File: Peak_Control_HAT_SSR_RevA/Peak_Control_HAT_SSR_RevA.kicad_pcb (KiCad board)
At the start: 4 copper layers, 115 x 70 mm, 19 parts, among them J1 Raspberry Pi 40-pin stacking 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, J11 I2C: 3V3 / GND / SDA / SCL, J2 24V IN: +24V / 0V, J3 PROJECTOR: SW+24V / 0V, J4 VIEWER: SW+24V / 0V, J5 AUX1: SW+24V / 0V, J6 AUX2: SW+24V / 0V, U1 G3VM-61GR2, U2 G3VM-61GR2, U3 G3VM-61GR2, U4 G3VM-61GR2

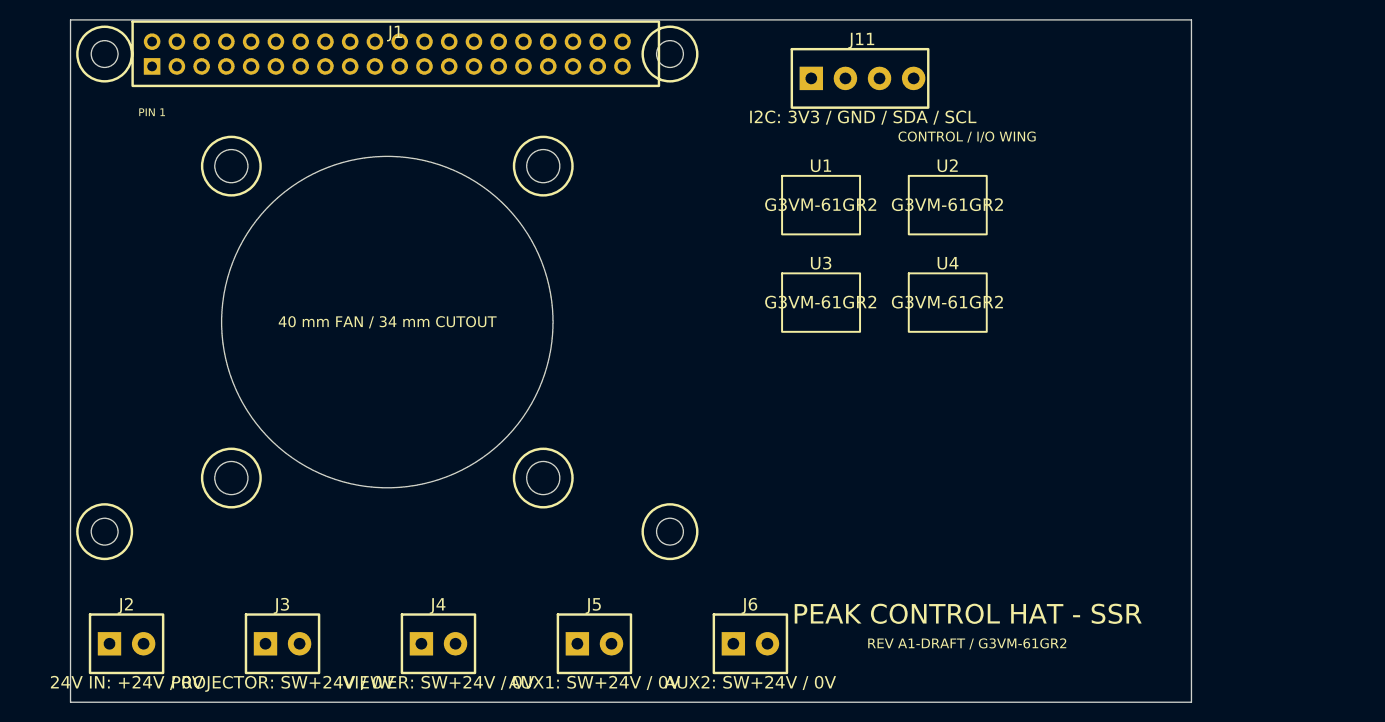
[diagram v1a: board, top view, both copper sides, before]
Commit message: Finalized Rev A component placement before routing
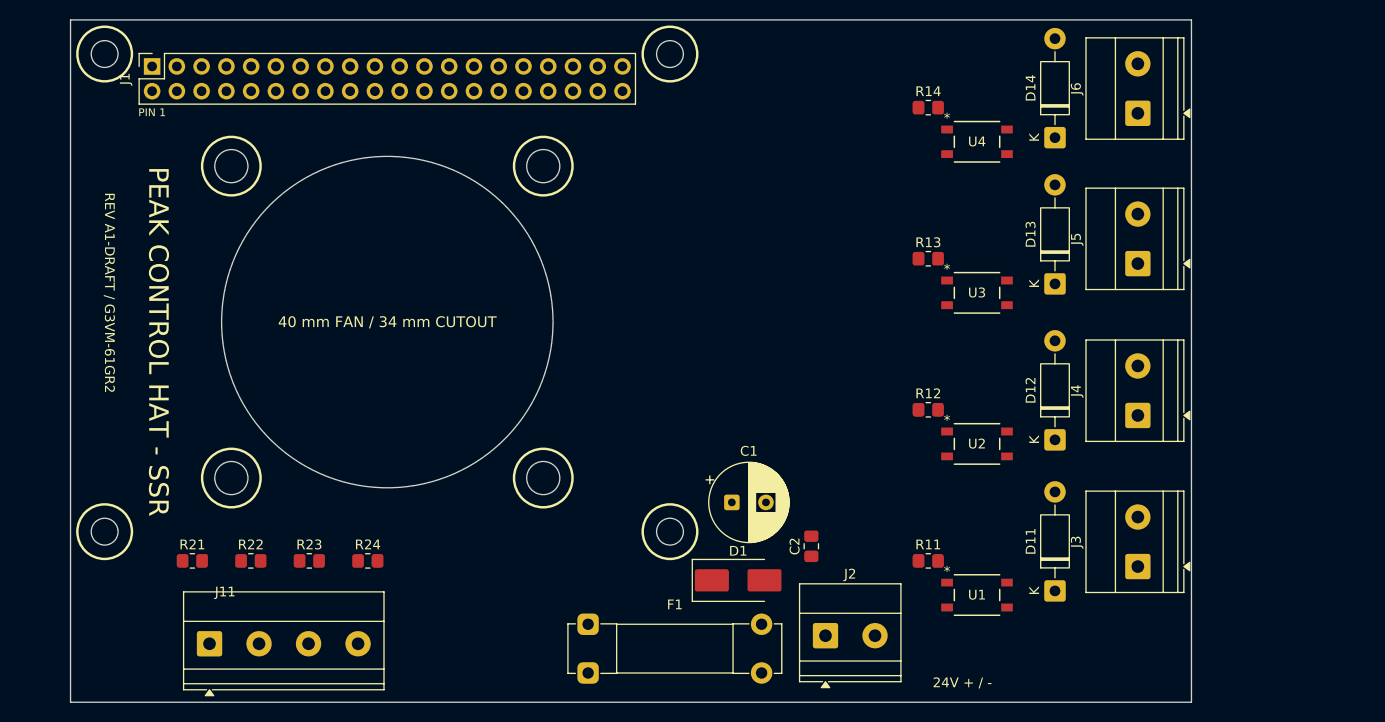
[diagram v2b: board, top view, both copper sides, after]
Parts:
- added C1: 47uF/50V, Capacitor_THT:CP_Radial_D8.0mm_P3.50mm, F.Cu at (67.8, 49.5)
- added C2: 1uF/50V, Capacitor_SMD:C_0805_2012Metric_Pad1.18x1.45mm_HandSolder, F.Cu at (76.0, 54.0)
- added D1: SMBJ33A, Diode_SMD:D_SMB_Handsoldering, F.Cu at (68.5, 57.5)
- added D11: 1N4007, Diode_THT:D_DO-41_SOD81_P10.16mm_Horizontal, F.Cu at (101.0, 58.6)
- added D12: 1N4007, Diode_THT:D_DO-41_SOD81_P10.16mm_Horizontal, F.Cu at (101.0, 43.1)
- added D13: 1N4007, Diode_THT:D_DO-41_SOD81_P10.16mm_Horizontal, F.Cu at (101.0, 27.1)
- added D14: 1N4007, Diode_THT:D_DO-41_SOD81_P10.16mm_Horizontal, F.Cu at (101.0, 12.1)
- added F1: 3A, Fuse:Fuseholder_Clip-5x20mm_Bel_FC-203-22_Lateral_P17.80x5.00mm_D1.17mm_Horizontal, F.Cu at (53.1, 62.0)
- added R11: 390R, Resistor_SMD:R_0805_2012Metric_Pad1.20x1.40mm_HandSolder, F.Cu at (88.0, 55.5)
- added R12: 390R, Resistor_SMD:R_0805_2012Metric_Pad1.20x1.40mm_HandSolder, F.Cu at (88.0, 40.0)
- added R13: 390R, Resistor_SMD:R_0805_2012Metric_Pad1.20x1.40mm_HandSolder, F.Cu at (88.0, 24.5)
- added R14: 390R, Resistor_SMD:R_0805_2012Metric_Pad1.20x1.40mm_HandSolder, F.Cu at (88.0, 9.00)
- added R21: DNP 4.7k SDA PU, Resistor_SMD:R_0805_2012Metric_Pad1.20x1.40mm_HandSolder, F.Cu at (12.5, 55.5)
- added R22: DNP 4.7k SCL PU, Resistor_SMD:R_0805_2012Metric_Pad1.20x1.40mm_HandSolder, F.Cu at (18.5, 55.5)
- added R23: 0R/optional 33-100R SDA, Resistor_SMD:R_0805_2012Metric_Pad1.20x1.40mm_HandSolder, F.Cu at (24.5, 55.5)
- added R24: 0R/optional 33-100R SCL, Resistor_SMD:R_0805_2012Metric_Pad1.20x1.40mm_HandSolder, F.Cu at (30.5, 55.5)
- J1: value Raspberry Pi 40-pin stacking header -> Raspberry Pi 40-Pin GPIO Header; footprint Peak:Raspberry_Pi_2x20_Header -> Connector_PinSocket_2.54mm:PinSocket_2x20_P2.54mm_Vertical
- J11: value I2C: 3V3 / GND / SDA / SCL -> I2C_EXPANSION; footprint Peak:Pluggable_Terminal_4P_3.5mm -> TerminalBlock_Phoenix:TerminalBlock_Phoenix_MKDS-1,5-4-5.08_1x04_P5.08mm_Horizontal
- J2: value 24V IN: +24V / 0V -> 24V_IN; footprint Peak:Pluggable_Terminal_2P_3.5mm -> TerminalBlock_Phoenix:TerminalBlock_Phoenix_MKDS-1,5-2-5.08_1x02_P5.08mm_Horizontal
- J3: value PROJECTOR: SW+24V / 0V -> PROJECTOR_SW24V_GND; footprint Peak:Pluggable_Terminal_2P_3.5mm -> TerminalBlock_Phoenix:TerminalBlock_Phoenix_MKDS-1,5-2-5.08_1x02_P5.08mm_Horizontal
- J4: value VIEWER: SW+24V / 0V -> VIEWER_SW24V_GND; footprint Peak:Pluggable_Terminal_2P_3.5mm -> TerminalBlock_Phoenix:TerminalBlock_Phoenix_MKDS-1,5-2-5.08_1x02_P5.08mm_Horizontal
- J5: value AUX1: SW+24V / 0V -> AUX1_SW24V_GND; footprint Peak:Pluggable_Terminal_2P_3.5mm -> TerminalBlock_Phoenix:TerminalBlock_Phoenix_MKDS-1,5-2-5.08_1x02_P5.08mm_Horizontal
- J6: value AUX2: SW+24V / 0V -> AUX2_SW24V_GND; footprint Peak:Pluggable_Terminal_2P_3.5mm -> TerminalBlock_Phoenix:TerminalBlock_Phoenix_MKDS-1,5-2-5.08_1x02_P5.08mm_Horizontal
- U1, U2, U3, U4: footprint Peak:G3VM-61GR2_PLACEHOLDER -> Omron:G-SOP4_OMR
- moved J3 89.8 mm to (109.5, 56.1), turned to 90 degrees
- moved J11 84.7 mm to (14.3, 64.0)
- moved J4 77.1 mm to (109.5, 40.6), turned to 90 degrees
- moved J2 73.5 mm to (77.5, 63.2)
- moved J5 69.5 mm to (109.5, 25.0), turned to 90 degrees
- moved J6 68.4 mm to (109.5, 9.58), turned to 90 degrees
- moved U1 40.8 mm to (89.9, 57.7)
- moved U2 23.2 mm to (89.9, 42.2)
- moved U4 17.8 mm to (89.9, 11.2)
- moved U3 13.1 mm to (89.9, 26.7)
- turned J1 to 90 degrees
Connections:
- J1 pad 1: (no net) -> /+3V3_PI
- J1 pad 10: (no net) -> unconnected-(J1-Pin_10-Pad10)
- J1 pad 11: (no net) -> unconnected-(J1-Pin_11-Pad11)
- J1 pad 12: (no net) -> unconnected-(J1-Pin_12-Pad12)
- J1 pad 13: (no net) -> unconnected-(J1-Pin_13-Pad13)
- J1 pad 14: (no net) -> /PI_GND
- J1 pad 15: (no net) -> /GPIO22_OUT3
- J1 pad 16: (no net) -> /GPIO23_OUT4
- J1 pad 17: (no net) -> unconnected-(J1-Pin_17-Pad17)
- J1 pad 18: (no net) -> unconnected-(J1-Pin_18-Pad18)
- J1 pad 19: (no net) -> unconnected-(J1-Pin_19-Pad19)
- J1 pad 2: (no net) -> unconnected-(J1-Pin_2-Pad2)
- J1 pad 20: (no net) -> /PI_GND
- J1 pad 21: (no net) -> unconnected-(J1-Pin_21-Pad21)
- J1 pad 22: (no net) -> unconnected-(J1-Pin_22-Pad22)
- J1 pad 23: (no net) -> unconnected-(J1-Pin_23-Pad23)
- J1 pad 24: (no net) -> unconnected-(J1-Pin_24-Pad24)
- J1 pad 25: (no net) -> /PI_GND
- J1 pad 26: (no net) -> unconnected-(J1-Pin_26-Pad26)
- J1 pad 27: (no net) -> unconnected-(J1-Pin_27-Pad27)
- J1 pad 28: (no net) -> unconnected-(J1-Pin_28-Pad28)
- J1 pad 29: (no net) -> unconnected-(J1-Pin_29-Pad29)
- J1 pad 3: (no net) -> /I2C_SDA_GPIO2
- J1 pad 30: (no net) -> /PI_GND
- J1 pad 31: (no net) -> unconnected-(J1-Pin_31-Pad31)
- J1 pad 32: (no net) -> unconnected-(J1-Pin_32-Pad32)
- J1 pad 33: (no net) -> unconnected-(J1-Pin_33-Pad33)
- J1 pad 34: (no net) -> /PI_GND
- J1 pad 35: (no net) -> /GPIO19_OUT2
- J1 pad 36: (no net) -> /GPIO16_OUT1
- J1 pad 37: (no net) -> unconnected-(J1-Pin_37-Pad37)
- J1 pad 38: (no net) -> unconnected-(J1-Pin_38-Pad38)
- J1 pad 39: (no net) -> /PI_GND
- J1 pad 4: (no net) -> unconnected-(J1-Pin_4-Pad4)
- J1 pad 40: (no net) -> unconnected-(J1-Pin_40-Pad40)
- J1 pad 5: (no net) -> /I2C_SCL_GPIO3
- J1 pad 6: (no net) -> /PI_GND
- J1 pad 7: (no net) -> unconnected-(J1-Pin_7-Pad7)
- J1 pad 8: (no net) -> unconnected-(J1-Pin_8-Pad8)
- J1 pad 9: (no net) -> /PI_GND
- J11 pad 1: (no net) -> /+3V3_PI
- J11 pad 2: (no net) -> /PI_GND
- J11 pad 3: (no net) -> /I2C_SDA_EXT
- J11 pad 4: (no net) -> /I2C_SCL_EXT
- J2 pad 1: (no net) -> Net-(J2-Pin_1)
- J2 pad 2: (no net) -> /FIELD_GND
- J3 pad 1: (no net) -> /OUT1_SW
- J3 pad 2: (no net) -> /FIELD_GND
- J4 pad 1: (no net) -> /OUT2_SW
- J4 pad 2: (no net) -> /FIELD_GND
- J5 pad 1: (no net) -> /OUT3_SW
- J5 pad 2: (no net) -> /FIELD_GND
- J6 pad 1: (no net) -> /OUT4_SW
- J6 pad 2: (no net) -> /FIELD_GND
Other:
- board text added: "24V + / -"
- board text removed: "CONTROL / I/O WING"

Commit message: Added most traces and zones
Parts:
- added C31: 22uF 50V, Capacitor_THT:CP_Radial_D5.0mm_P2.00mm, F.Cu at (69.5, 38.0)
- added C32: 47uF 16V, Capacitor_THT:CP_Radial_D5.0mm_P2.00mm, F.Cu at (51.0, 56.5)
- added J12: Fan 5V, Connector_JST:JST_XH_B2B-XH-A_1x02_P2.50mm_Vertical, F.Cu at (41.0, 60.0)
- added U5: OKI-78SR-5_1.5-W36-C, Converter_DCDC:Converter_DCDC_Murata_OKI-78SR_Vertical, F.Cu at (59.0, 37.5)
- moved D11 0.50 mm to (100.5, 58.6)
- moved D12 0.50 mm to (100.5, 43.1)
- moved D13 0.50 mm to (100.5, 27.1)
- moved D14 0.50 mm to (100.5, 12.1)
- turned R11 to 180 degrees
- turned R12 to 180 degrees
- turned R13 to 180 degrees
- turned R14 to 180 degrees
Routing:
- net /+24V_FIELD: track 0.00 -> 176.8 mm
- net /PI_GND: track 0.00 -> 78.3 mm, vias 0 -> 12
- net /FIELD_GND: track 0.00 -> 70.2 mm
- net /GPIO22_OUT3: track 0.00 -> 70.0 mm, vias 0 -> 2
- net /GPIO23_OUT4: track 0.00 -> 69.6 mm, vias 0 -> 1
- net /GPIO16_OUT1: track 0.00 -> 62.9 mm, vias 0 -> 1
- net /GPIO19_OUT2: track 0.00 -> 50.9 mm, vias 0 -> 1
- net /+5V_FAN: track 0.00 -> 29.1 mm
- net /OUT2_SW: track 0.00 -> 14.8 mm
- net /OUT1_SW: track 0.00 -> 14.8 mm
- net /OUT4_SW: track 0.00 -> 14.8 mm
- net /OUT3_SW: track 0.00 -> 14.4 mm
- net Net-(J2-Pin_1): track 0.00 -> 12.0 mm
- net Net-(R14-Pad1): track 0.00 -> 2.61 mm
- net Net-(R13-Pad1): track 0.00 -> 2.61 mm
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- added copper zone on In1.Cu, net /FIELD_GND
- added copper zone on In1.Cu, net /PI_GND
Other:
- board text added: "+ / -"
- board text added: "24V Input"
- board text removed: "24V + / -"

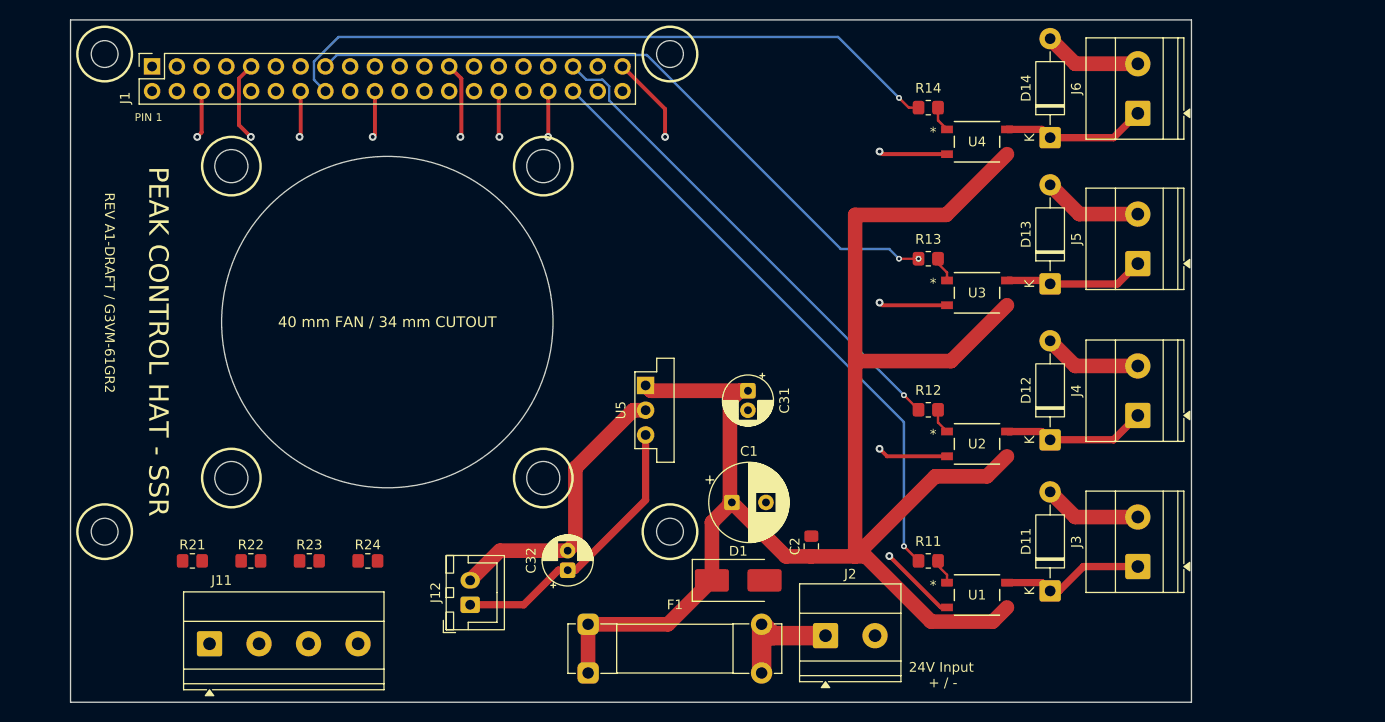
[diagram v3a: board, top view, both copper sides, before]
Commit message: Finished all traces, still needs full inspection
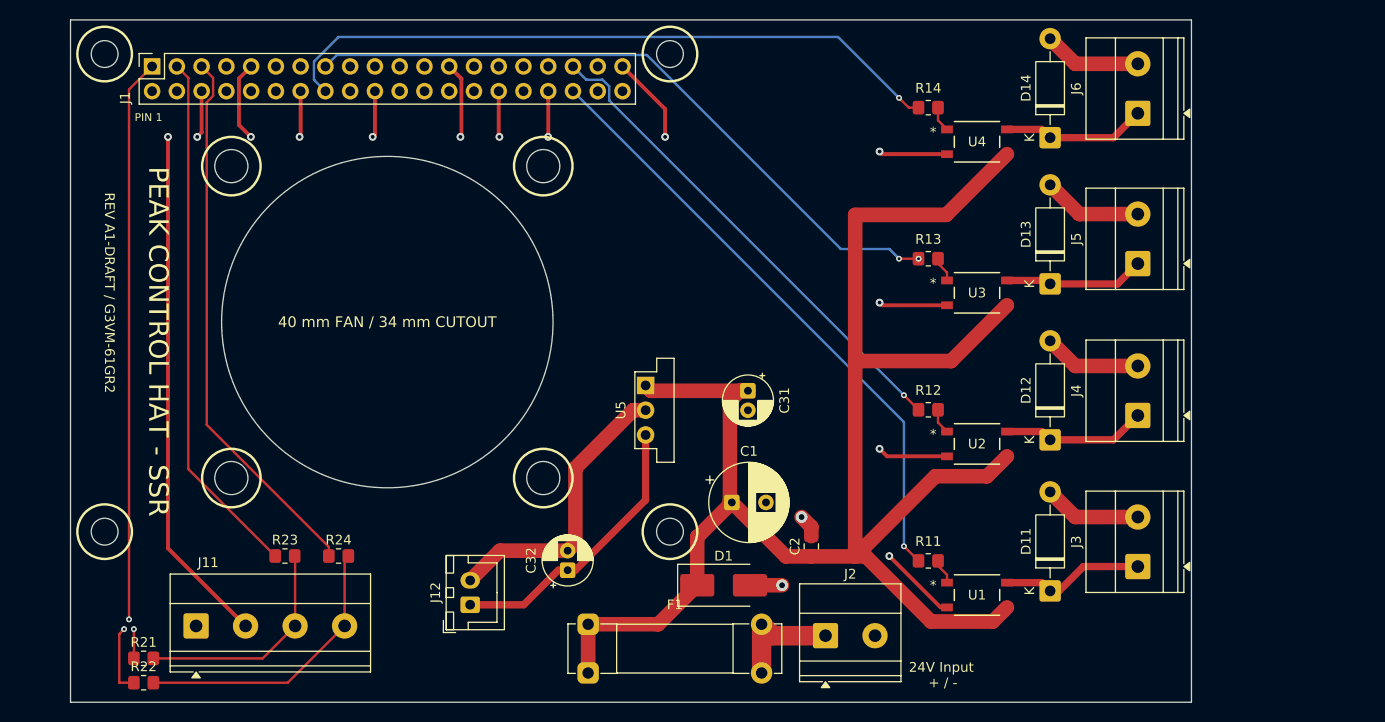
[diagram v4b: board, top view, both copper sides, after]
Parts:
- moved R22 16.7 mm to (7.50, 68.0)
- moved R21 11.2 mm to (7.50, 65.5)
- moved R24 3.04 mm to (27.5, 55.0)
- moved R23 2.55 mm to (22.0, 55.0)
- moved J11 2.29 mm to (12.9, 62.2)
- moved D1 1.58 mm to (67.0, 58.0)
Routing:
- net /+3V3_PI: track 0.00 -> 67.9 mm, vias 0 -> 3
- net /I2C_SCL_GPIO3: track 0.00 -> 56.2 mm
- net /I2C_SDA_GPIO2: track 0.00 -> 54.4 mm
- net /PI_GND: track 78.3 -> 131.8 mm, vias 12 -> 13
- net /I2C_SCL_EXT: track 0.00 -> 29.4 mm
- net /I2C_SDA_EXT: track 0.00 -> 23.1 mm
- net /FIELD_GND: track 70.2 -> 75.9 mm, vias 0 -> 2
- net /+24V_FIELD: track 176.8 -> 176.2 mm
- added copper zone on In1.Cu, net /+3V3_PI

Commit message: Fixed a few traces and silkscreen placements, still requires full inspection
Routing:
- net /GPIO22_OUT3: vias 2 -> 1

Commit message: Added pulldown resistors for SSRs
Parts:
- added R15: 100K, Resistor_SMD:R_0805_2012Metric_Pad1.20x1.40mm_HandSolder, F.Cu at (87.0, 54.0)
- added R16: 100K, Resistor_SMD:R_0805_2012Metric_Pad1.20x1.40mm_HandSolder, F.Cu at (85.0, 42.5)
- added R17: 100K, Resistor_SMD:R_0805_2012Metric_Pad1.20x1.40mm_HandSolder, F.Cu at (84.5, 27.5)
- added R18: 100K, Resistor_SMD:R_0805_2012Metric_Pad1.20x1.40mm_HandSolder, F.Cu at (82.0, 9.00)
- moved R11 3.35 mm to (91.0, 54.0), turned to 90 degrees
- moved R12 1.12 mm to (89.0, 39.5)
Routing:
- net /PI_GND: track 131.8 -> 147.2 mm
- net /GPIO19_OUT2: track 50.9 -> 55.9 mm
- net /GPIO22_OUT3: track 70.0 -> 73.2 mm
- net /GPIO16_OUT1: track 62.9 -> 65.4 mm
- net /GPIO23_OUT4: track 69.6 -> 72.0 mm
- net Net-(R11-Pad1): track 2.61 -> 3.18 mm

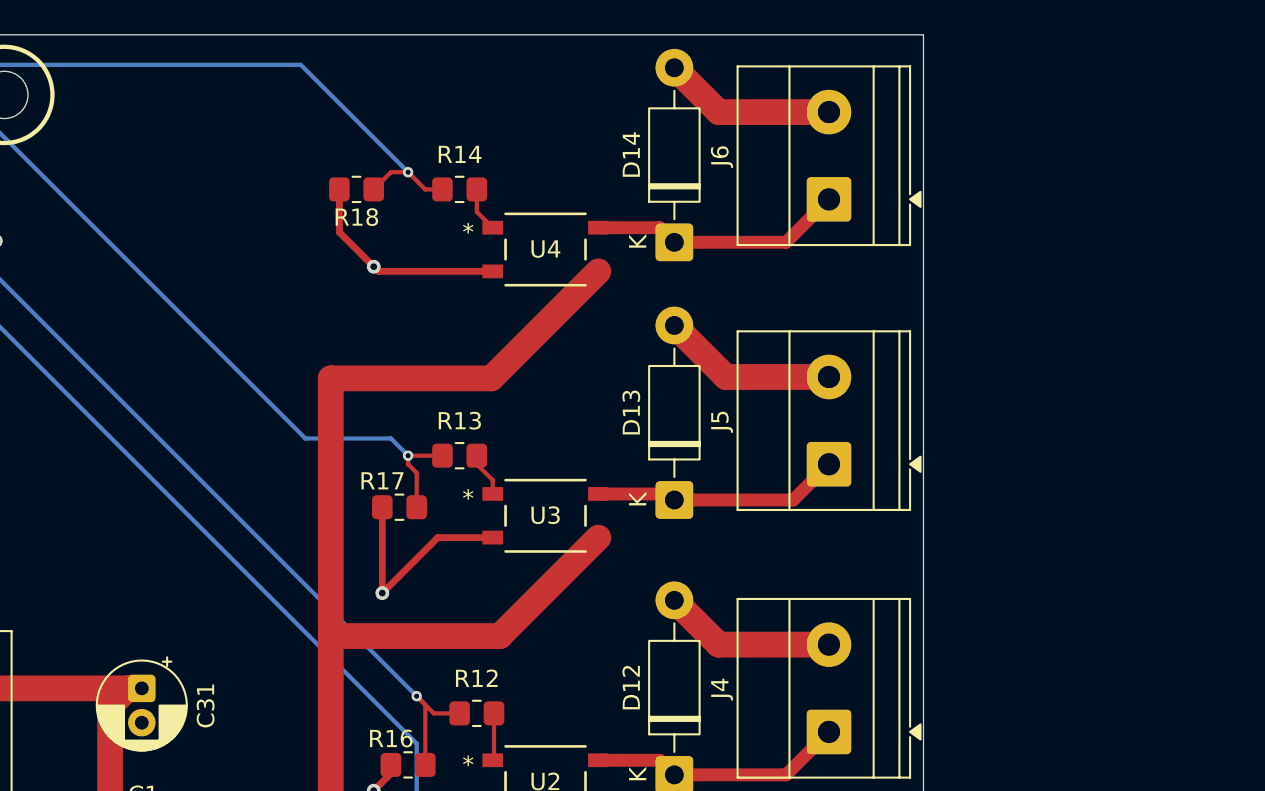
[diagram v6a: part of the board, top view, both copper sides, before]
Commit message: Created Peak_Control_SSR_Interface project for V1
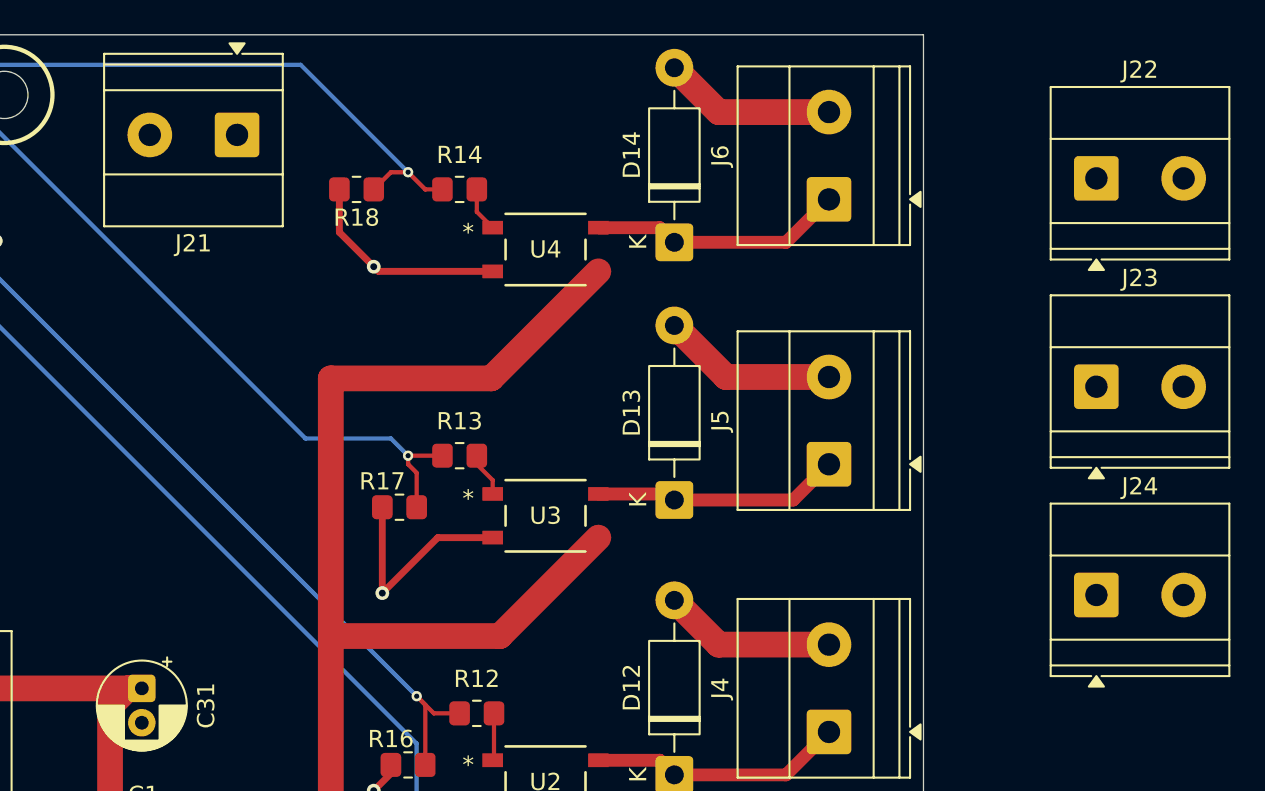
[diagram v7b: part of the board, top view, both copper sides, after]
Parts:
- added J21: POR1, TerminalBlock_Phoenix:TerminalBlock_Phoenix_MKDS-1,5-2-5.08_1x02_P5.08mm_Horizontal, F.Cu at (75.0, 5.83)
- added J22: POR2, TerminalBlock_Phoenix:TerminalBlock_Phoenix_MKDS-1,5-2-5.08_1x02_P5.08mm_Horizontal, F.Cu at (125.1, 8.36)
- added J23: IR1, TerminalBlock_Phoenix:TerminalBlock_Phoenix_MKDS-1,5-2-5.08_1x02_P5.08mm_Horizontal, F.Cu at (125.1, 20.5)
- added J24: IR2, TerminalBlock_Phoenix:TerminalBlock_Phoenix_MKDS-1,5-2-5.08_1x02_P5.08mm_Horizontal, F.Cu at (125.1, 32.6)
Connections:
- J1 pad 11: unconnected-(J1-Pin_11-Pad11) -> /GPIO17_IR1
- J1 pad 12: unconnected-(J1-Pin_12-Pad12) -> /GPIO18_IR2
- J1 pad 18: unconnected-(J1-Pin_18-Pad18) -> /GPIO24_POR1
- J1 pad 22: unconnected-(J1-Pin_22-Pad22) -> /GPIO25_POR2
